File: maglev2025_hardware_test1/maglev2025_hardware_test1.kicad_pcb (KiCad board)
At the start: 2 copper layers, 100 x 100 mm, 100 parts, among them J1 SWD, J2 PWRIn, U1 RY8411, U10 INA240A1PW, U11 INA240A1PW, U12 INA240A1PW, U2 TMAG5170-Q1, U3 STM32G474RBTx, U4 RS3236, U5 AT8236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

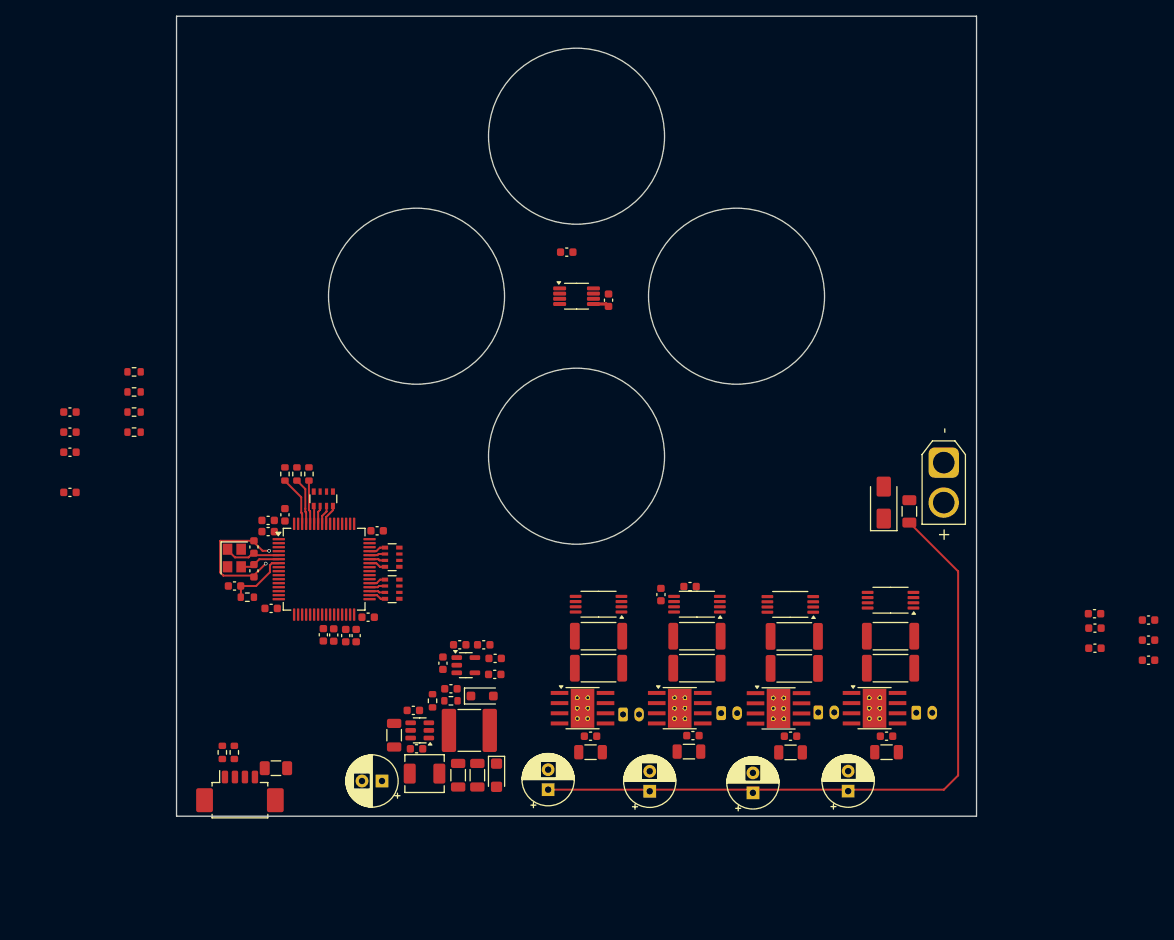
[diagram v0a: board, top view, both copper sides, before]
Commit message: Layout routing done, checking test
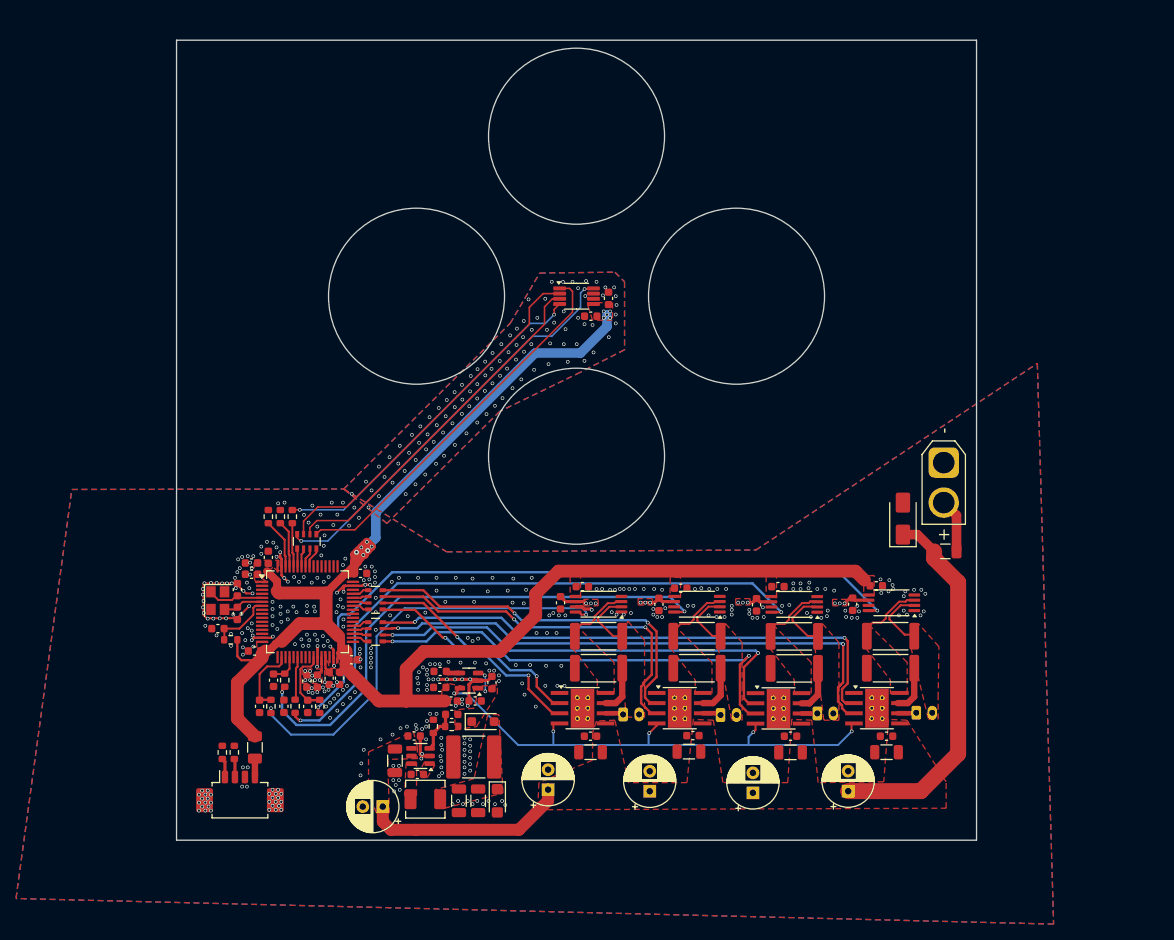
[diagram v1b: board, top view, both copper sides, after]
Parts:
- moved C44 58.6 mm to (113.0, 136.5)
- moved C48 54.5 mm to (110.3, 138.5), turned to -90 degrees
- moved C45 46.8 mm to (125.2, 136.3)
- moved R7 45.2 mm to (61.8, 151.3), turned to 90 degrees
- moved C35 43.8 mm to (60.4, 151.3), turned to 90 degrees
- moved C49 42.4 mm to (122.5, 138.6), turned to -90 degrees
- moved R9 41.9 mm to (64.8, 151.3), turned to 90 degrees
- moved C37 41.5 mm to (63.4, 151.3), turned to 90 degrees
- moved R10 41.4 mm to (67.9, 151.3), turned to 90 degrees
- moved R8 40.7 mm to (63.5, 148.0), turned to 90 degrees
- moved C36 40.1 mm to (62.1, 148.0), turned to 90 degrees
- moved C38 40.0 mm to (66.4, 151.3), turned to 90 degrees
- moved C46 35.3 mm to (137.5, 136.2)
- moved C50 30.8 mm to (134.5, 138.5), turned to -90 degrees
- moved C43 13.5 mm to (100.7, 136.3)
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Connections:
- C35 pad 2: ISENSE_A -> ISENSE_A_MCU
- C36 pad 2: ISENSE_B -> ISENSE_B_MCU
- C37 pad 2: ISENSE_C -> ISENSE_C_MCU
- C38 pad 2: ISENSE_D -> ISENSE_D_MCU
- R10 pad 1: ISENSE_D_MCU -> ISENSE_D
- R10 pad 2: ISENSE_D -> ISENSE_D_MCU
- R4 pad 2: LIS3_CS -> ~{MAG_CS}
- R7 pad 1: ISENSE_A_MCU -> ISENSE_A
- R7 pad 2: ISENSE_A -> ISENSE_A_MCU
- R8 pad 1: ISENSE_B_MCU -> ISENSE_B
- R8 pad 2: ISENSE_B -> ISENSE_B_MCU
- R9 pad 1: ISENSE_C_MCU -> ISENSE_C
- R9 pad 2: ISENSE_C -> ISENSE_C_MCU
- RN2 pad 8: LIS3_DRY -> ~{MAG_ALRT}
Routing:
- net +3.3V: track 2.01 -> 261.0 mm, vias 0 -> 16
- net VREF: track 0.00 -> 87.5 mm, vias 0 -> 19
- net ISENSE_D: track 0.00 -> 86.4 mm, vias 0 -> 2
- net ISENSE_C: track 0.00 -> 75.6 mm, vias 0 -> 2
- net CTRL_D1: track 0.00 -> 69.1 mm, vias 0 -> 2
- net CTRL_D2: track 0.00 -> 68.6 mm, vias 0 -> 2
- net ISENSE_B: track 0.00 -> 67.1 mm, vias 0 -> 2
- net CTRL_C1: track 0.00 -> 56.9 mm, vias 0 -> 2
- net CTRL_C2: track 0.00 -> 56.8 mm, vias 0 -> 2
- net ISENSE_A: track 0.00 -> 54.4 mm, vias 0 -> 2
- net ~{MAG_ALRT}: track 0.00 -> 51.8 mm, vias 0 -> 2
- net SPI1_SCK: track 0.00 -> 47.9 mm
- net CTRL_B1: track 0.00 -> 47.3 mm, vias 0 -> 2
- net CTRL_B2: track 0.00 -> 47.0 mm, vias 0 -> 2
- net SPI1_MOSI: track 0.00 -> 46.7 mm
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- added copper zone on F.Cu, net +3.3V
- added copper zone on F.Cu, net /5V
- added copper zone on B.Cu, net GND
- added copper zone on F.Cu, net GND
- added copper zone on In1.Cu, net GND
- added copper zone on In2.Cu, net GND
- added copper zone on F.Cu, net Net-(D2-A1)
- added copper zone on F.Cu, net Net-(L2-+)
- added copper zone on F.Cu, net Net-(L3-+)
- added copper zone on F.Cu, net Net-(L4-+)
- added copper zone on F.Cu, net Net-(L5-+)
- added copper zone on F.Cu, net Net-(U1-BS)
- added copper zone on F.Cu, net Net-(U1-LX)
- added copper zone on F.Cu, net Net-(U10--)
- added copper zone on F.Cu, net Net-(U11--)
- added copper zone on F.Cu, net Net-(U12--)
- added copper zone on F.Cu, net Net-(U5-OUT2)
- added copper zone on F.Cu, net VPP
- added copper zone on F.Cu, net VREF
- added copper zone on In2.Cu, net VREF
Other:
- outline, holes or cut-outs redrawn
- copper layers 2 -> 4

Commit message: Almost Complete
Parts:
- added H1: MountingHole_Pad, MountingHole:MountingHole_3.2mm_M3_DIN965_Pad_TopBottom, F.Cu at (140.0, 100.0)
- added H2: MountingHole_Pad, MountingHole:MountingHole_3.2mm_M3_DIN965_Pad_TopBottom, F.Cu at (130.0, 120.0)
- added H3: MountingHole_Pad, MountingHole:MountingHole_3.2mm_M3_DIN965_Pad_TopBottom, F.Cu at (120.0, 80.0)
- added H4: MountingHole_Pad, MountingHole:MountingHole_3.2mm_M3_DIN965_Pad_TopBottom, F.Cu at (60.0, 100.0)
- added H5: MountingHole_Pad, MountingHole:MountingHole_3.2mm_M3_DIN965_Pad_TopBottom, F.Cu at (70.0, 120.0)
- added H6: MountingHole_Pad, MountingHole:MountingHole_3.2mm_M3_DIN965_Pad_TopBottom, F.Cu at (80.0, 80.0)
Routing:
- net Net-(U3-PA14): track 0.00 -> 35.2 mm, vias 0 -> 2
- net Net-(U3-PA15): track 0.00 -> 34.8 mm, vias 0 -> 2
- net ISENSE_C_MCU: track 5.18 -> 6.60 mm
- net VREF: track 87.5 -> 88.7 mm
- net GND: vias 509 -> 603
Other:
- outline, holes or cut-outs redrawn
- board text added: "DC-+"
- board text added: "MAGLEV2025_V0.1 ELEC3300 Proj by RY OFR"
- board text added: "TMAG5170"
- board text added: "X"
- board text added: "Y"
- board text added: "Z"

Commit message: ver 0.1 sent to fabrication
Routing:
- net GND: vias 603 -> 636
